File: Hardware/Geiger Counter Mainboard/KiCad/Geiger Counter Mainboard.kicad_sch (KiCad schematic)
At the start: 33 parts, among them J1 MAIN TUBE(S), J2 FOLLOWER TUBE(S), J3 USB, Q1 MMBT3904, Q2 MMBT3906, Q3 MMBT3904, Q4 MMBT3906, Q5 MMBT3904, Q6 MMBT3904, Q7 MMBT3904, Q8 MMBT3904

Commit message: Updated TFT module footprint
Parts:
- renumbered J2 to J1, J1 to J2, R14 to R13, R13 to R14, R5 to R2, R2 to R3, R3 to R4, R4 to R5
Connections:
- net MISO: now also U2.17 (SD_MISO)
- net MOSI: now also U2.16 (SD_MOSI)
- net SCLK: now also U2.18 (SD_SCLK)
- net SD_CS: now reaches U1.10 (17)
- net SD_CS: now also U2.15 (SD_CS)
- no-connect marks 22 -> 21

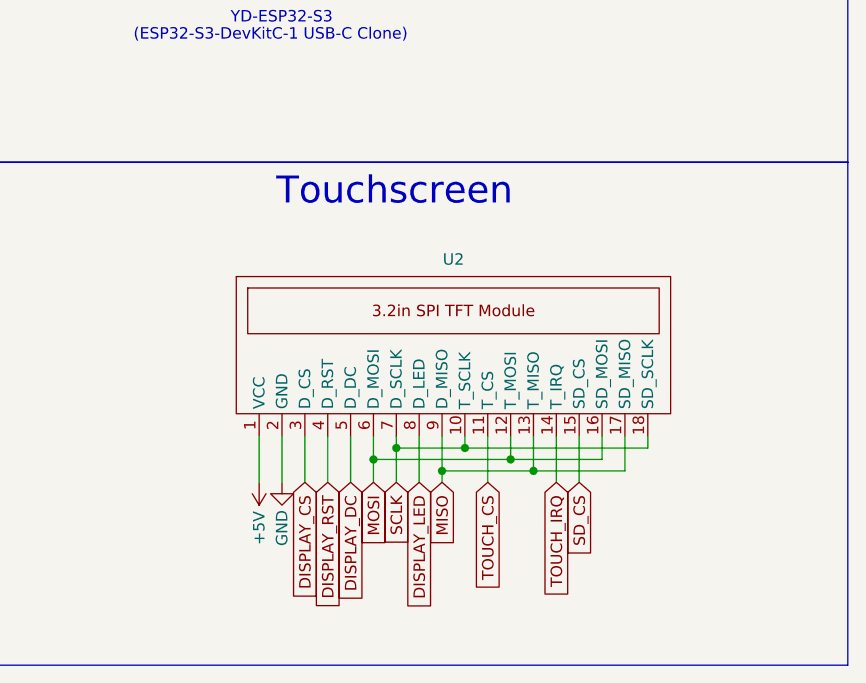
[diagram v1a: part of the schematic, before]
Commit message: Updated TFT module footprint & schematic
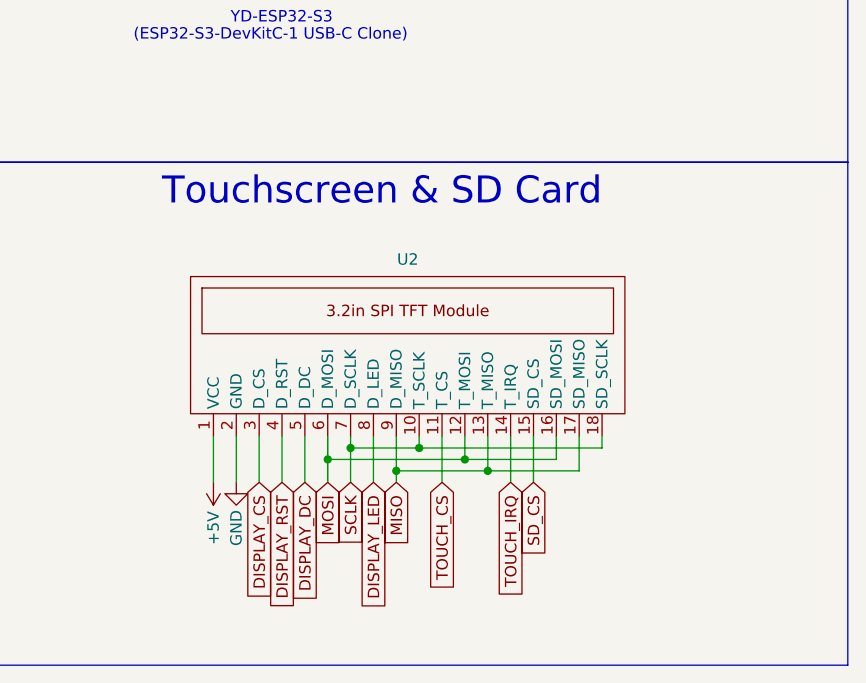
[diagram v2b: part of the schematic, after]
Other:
- note added: "Touchscreen & SD Card"
- note removed: "Touchscreen"
- moved on the sheet: U2

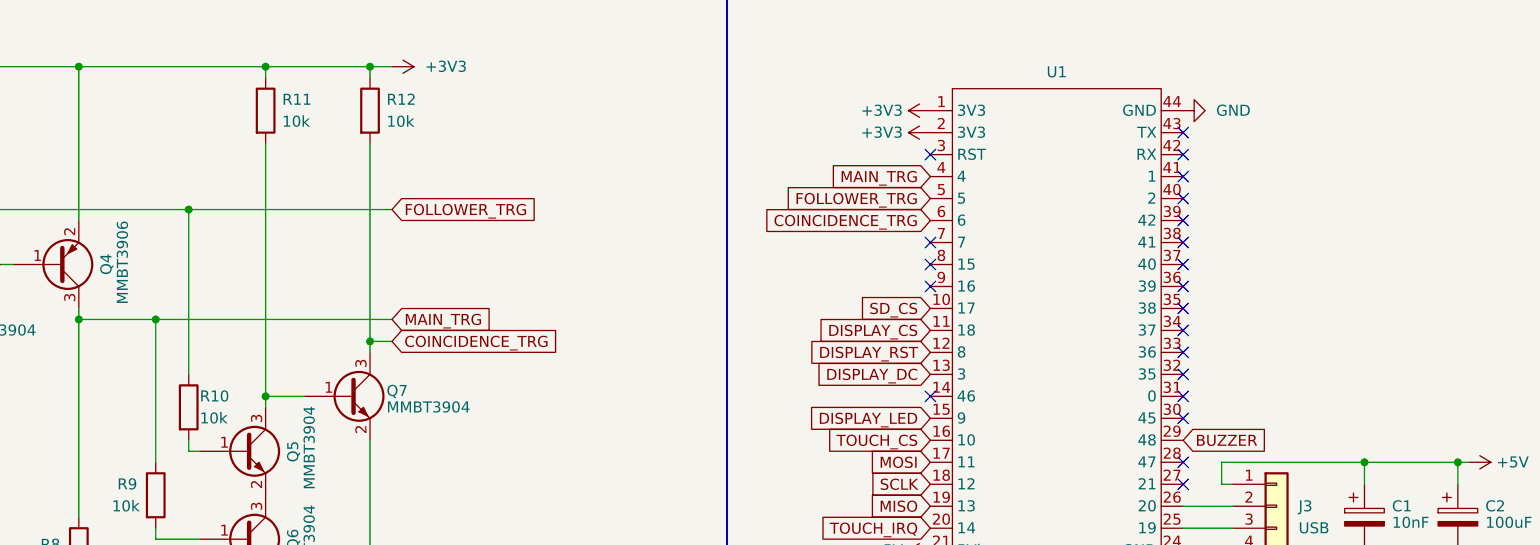
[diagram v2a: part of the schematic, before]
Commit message: Updated schematic & set PCB properties
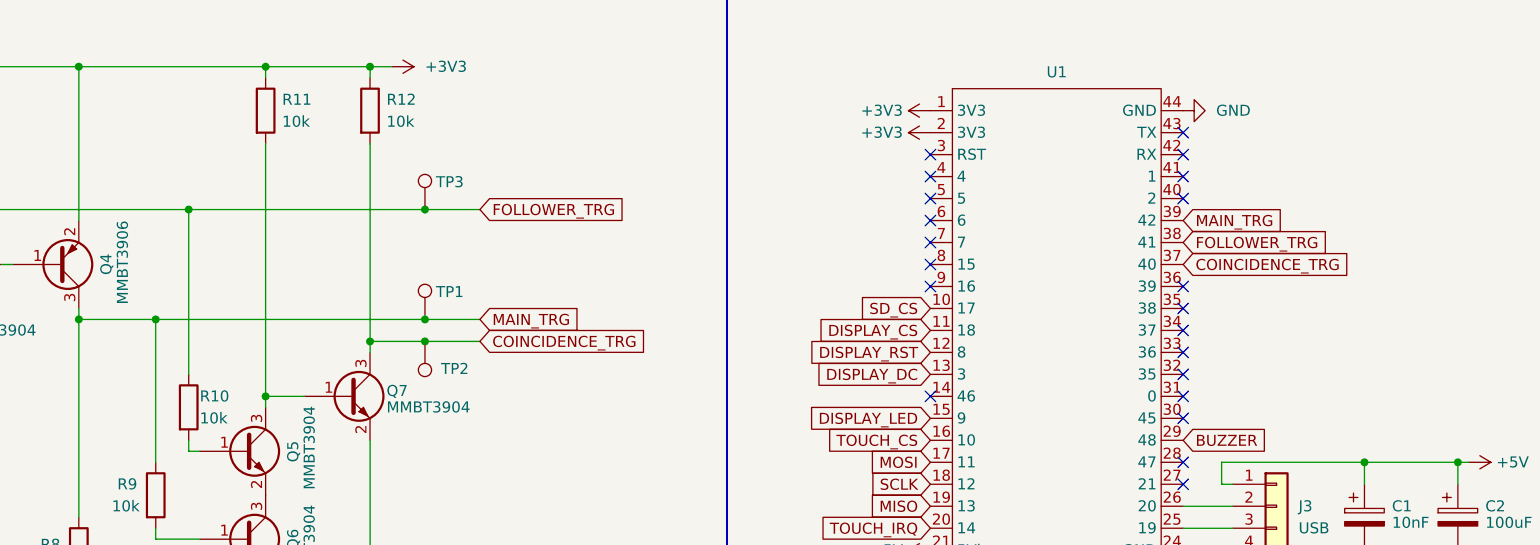
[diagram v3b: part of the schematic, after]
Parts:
- added TP1, TP2, TP3: TestPoint, TestPoint:TestPoint_Pad_D1.5mm, symbol Connector:TestPoint
- BZ1: footprint Connector_PinHeader_2.54mm:PinHeader_1x02_P2.54mm_Horizontal -> Connector_PinHeader_2.54mm:PinHeader_1x02_P2.54mm_Vertical
- J3: footprint Connector_PinHeader_2.54mm:PinHeader_1x04_P2.54mm_Horizontal -> Connector_PinHeader_2.54mm:PinHeader_1x04_P2.54mm_Vertical
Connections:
- net COINCIDENCE_TRG: now also U1.37 (40), TP2.1; no longer U1.6
- net FOLLOWER_TRG: now also U1.38 (41), TP3.1; no longer U1.5
- net MAIN_TRG: now also U1.39 (42), TP1.1; no longer U1.4

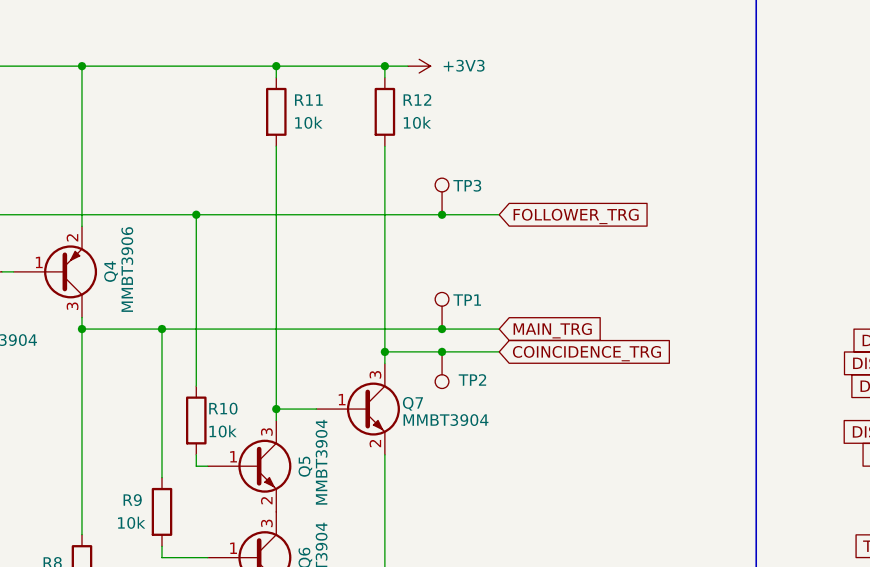
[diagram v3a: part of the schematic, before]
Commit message: Added PCB for mainboard
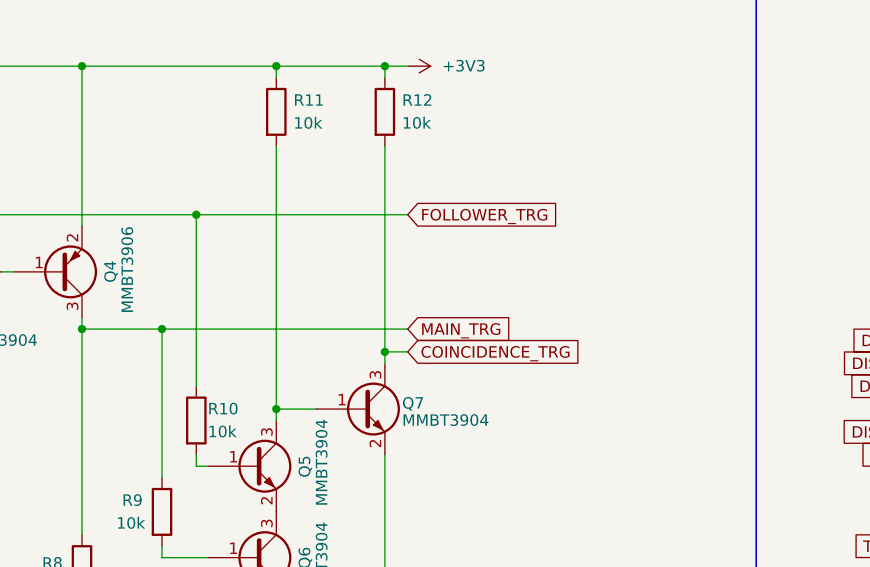
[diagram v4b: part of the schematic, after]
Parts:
- removed TP1, TP2, TP3: TestPoint, TestPoint:TestPoint_Pad_D1.5mm, symbol Connector:TestPoint
- J1, J2: footprint Connector_PinHeader_2.54mm:PinHeader_1x03_P2.54mm_Horizontal -> Connector_PinHeader_2.54mm:PinHeader_1x03_P2.54mm_Vertical
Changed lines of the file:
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@@
   (junction (at 132.715 67.945) (diameter 0) (color 0 0 0 0)
   )
-  (junction (at 151.13 59.055) (diameter 0) (color 0 0 0 0)
-  )
   (junction (at 93.345 90.805) (diameter 0) (color 0 0 0 0)
   )
@@
   (junction (at 144.78 29.845) (diameter 0) (color 0 0 0 0)
   )
-  (junction (at 151.13 61.595) (diameter 0) (color 0 0 0 0)
-  )
   (junction (at 245.11 144.145) (diameter 0) (color 0 0 0 0)
   )
@@
   )
   (junction (at 237.49 141.605) (diameter 0) (color 0 0 0 0)
-  )
-  (junction (at 151.13 46.355) (diameter 0) (color 0 0 0 0)
   )
   (junction (at 144.78 61.595) (diameter 0) (color 0 0 0 0)
@@
     (stroke (width 0) (type default))
   )
-  (wire (pts (xy 120.015 59.055) (xy 151.13 59.055))
+  (wire (pts (xy 120.015 59.055) (xy 147.32 59.055))
     (stroke (width 0) (type default))
   )
@@
     (stroke (width 0) (type default))
   )
-  (wire (pts (xy 151.13 46.355) (xy 157.48 46.355))
-    (stroke (width 0) (type default))
-  )
-  (wire (pts (xy 151.13 59.055) (xy 157.48 59.055))
-    (stroke (width 0) (type default))
-  )
   (wire (pts (xy 60.325 90.805) (xy 60.325 89.535))
     (stroke (width 0) (type default))
@@
     (stroke (width 0) (type default))
   )
-  (wire (pts (xy 144.78 61.595) (xy 151.13 61.595))
-    (stroke (width 0) (type default))
-  )
   (wire (pts (xy 252.73 140.335) (xy 252.73 142.875))
     (stroke (width 0) (type default))
@@
     (stroke (width 0) (type default))
   )
-  (wire (pts (xy 123.825 46.355) (xy 151.13 46.355))
+  (wire (pts (xy 123.825 46.355) (xy 147.32 46.355))
     (stroke (width 0) (type default))
   )
@@
     (stroke (width 0) (type default))
   )
-  (wire (pts (xy 151.13 61.595) (xy 157.48 61.595))
-    (stroke (width 0) (type default))
-  )
   (wire (pts (xy 36.195 151.13) (xy 37.465 151.13))
     (stroke (width 0) (type default))
@@
   )
   (wire (pts (xy 94.615 52.705) (xy 93.345 52.705))
+    (stroke (width 0) (type default))
+  )
+  (wire (pts (xy 147.32 61.595) (xy 144.78 61.595))
     (stroke (width 0) (type default))
   )
@@
     )
   )
-  (global_label "MAIN_TRG" (shape input) (at 157.48 59.055 0) (fields_autoplaced)
+  (global_label "MAIN_TRG" (shape input) (at 147.32 59.055 0) (fields_autoplaced)
     (effects (font (size 1.27 1.27)) (justify left))
-    (property "Intersheetrefs" "${INTERSHEET_REFS}" (at 169.4157 59.055 0)
+    (property "Intersheetrefs" "${INTERSHEET_REFS}" (at 159.2557 59.055 0)
       (effects (font (size 1.27 1.27)) (justify left) hide)
     )
@@
     )
   )
-  (global_label "FOLLOWER_TRG" (shape input) (at 157.48 46.355 0) (fields_autoplaced)
+  (global_label "FOLLOWER_TRG" (shape input) (at 147.32 46.355 0) (fields_autoplaced)
     (effects (font (size 1.27 1.27)) (justify left))
-    (property "Intersheetrefs" "${INTERSHEET_REFS}" (at 174.6166 46.355 0)
+    (property "Intersheetrefs" "${INTERSHEET_REFS}" (at 164.4566 46.355 0)
       (effects (font (size 1.27 1.27)) (justify left) hide)
     )
@@
     )
   )
-  (global_label "COINCIDENCE_TRG" (shape input) (at 157.48 61.595 0) (fields_autoplaced)
+  (global_label "COINCIDENCE_TRG" (shape input) (at 147.32 61.595 0) (fields_autoplaced)
     (effects (font (size 1.27 1.27)) (justify left))
-    (property "Intersheetrefs" "${INTERSHEET_REFS}" (at 177.5195 61.595 0)
+    (property "Intersheetrefs" "${INTERSHEET_REFS}" (at 167.3595 61.595 0)
       (effects (font (size 1.27 1.27)) (justify left) hide)
     )
@@
     )
   )
-  (symbol (lib_id "Connector:TestPoint") (at 151.13 46.355 0) (unit 1)
-    (in_bom yes) (on_board yes) (dnp no)
-    (property "Reference" "TP3" (at 152.4 43.18 0)
-      (effects (font (size 1.27 1.27)) (justify left))
-    )
-    (property "Value" "TestPoint" (at 153.67 44.323 0)
-      (effects (font (size 1.27 1.27)) (justify left) hide)
-    )
-    (property "Footprint" "TestPoint:TestPoint_Pad_D1.5mm" (at 156.21 46.355 0)
-      (effects (font (size 1.27 1.27)) hide)
-    )
-    (property "Datasheet" "~" (at 156.21 46.355 0)
-      (effects (font (size 1.27 1.27)) hide)
-    )
-    (pin "1")
-    (instances
-      (project "Geiger Counter Mainboard"
-        (path "/efb798f5-5593-4ba1-9dbc-e1eef9908111"
-          (reference "TP3") (unit 1)
-        )
-      )
-    )
-  )
   (symbol (lib_id "power:+3V3") (at 209.55 37.465 90) (unit 1)
     (in_bom yes) (on_board yes) (dnp no) (fields_autoplaced)
@@
         (path "/efb798f5-5593-4ba1-9dbc-e1eef9908111"
           (reference "#PWR04") (unit 1)
-        )
-      )
-    )
-  )
-  (symbol (lib_id "Connector:TestPoint") (at 151.13 59.055 0) (unit 1)
-    (in_bom yes) (on_board yes) (dnp no)
-    (property "Reference" "TP1" (at 152.4 55.88 0)
-      (effects (font (size 1.27 1.27)) (justify left))
-    )
-    (property "Value" "TestPoint" (at 153.67 57.023 0)
-      (effects (font (size 1.27 1.27)) (justify left) hide)
-    )
-    (property "Footprint" "TestPoint:TestPoint_Pad_D1.5mm" (at 156.21 59.055 0)
-      (effects (font (size 1.27 1.27)) hide)
-    )
-    (property "Datasheet" "~" (at 156.21 59.055 0)
-      (effects (font (size 1.27 1.27)) hide)
-    )
-    (pin "1")
-    (instances
-      (project "Geiger Counter Mainboard"
-        (path "/efb798f5-5593-4ba1-9dbc-e1eef9908111"
-          (reference "TP1") (unit 1)
         )
       )
@@
       (effects (font (size 1.27 1.27)))
     )
-    (property "Footprint" "Connector_PinHeader_2.54mm:PinHeader_1x03_P2.54mm_Horizontal" (at 38.735 59.055 0)
+    (property "Footprint" "Connector_PinHeader_2.54mm:PinHeader_1x03_P2.54mm_Vertical" (at 38.735 59.055 0)
       (effects (font (size 1.27 1.27)) hide)
     )
@@
       (effects (font (size 1.27 1.27)))
     )
-    (property "Footprint" "Connector_PinHeader_2.54mm:PinHeader_1x03_P2.54mm_Horizontal" (at 38.735 46.355 0)
+    (property "Footprint" "Connector_PinHeader_2.54mm:PinHeader_1x03_P2.54mm_Vertical" (at 38.735 46.355 0)
       (effects (font (size 1.27 1.27)) hide)
     )
@@
         )
       )
-    )
-  )
-  (symbol (lib_id "Connector:TestPoint") (at 151.13 61.595 180) (unit 1)
-    (in_bom yes) (on_board yes) (dnp no)
-    (property "Reference" "TP2" (at 156.21 64.77 0)
-      (effects (font (size 1.27 1.27)) (justify left))
-    )
-    (property "Value" "TestPoint" (at 148.59 63.627 0)
-      (effects (font (size 1.27 1.27)) (justify left) hide)
-    )
-    (property "Footprint" "TestPoint:TestPoint_Pad_D1.5mm" (at 146.05 61.595 0)
-      (effects (font (size 1.27 1.27)) hide)
-    )
-    (property "Datasheet" "~" (at 146.05 61.595 0)
-      (effects (font (size 1.27 1.27)) hide)
-    )
-    (pin "1")
-    (instances
-      (project "Geiger Counter Mainboard"
-        (path "/efb798f5-5593-4ba1-9dbc-e1eef9908111"
-          (reference "TP2") (unit 1)
-        )
-      )
